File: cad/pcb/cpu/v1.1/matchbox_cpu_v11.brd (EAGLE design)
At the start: 40 x 32 mm, 61 parts, among them CN1 SM02B-SRSS-TB, P1 DF12-32-DP, P2 DF12-32-DP, Q1 FDN360P, Q2 FDN360P, U1 STM32F415R, U2 MCP1703, U3 MCP73831, U4 LTC2954-2, Y1 16MHz(9pF)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

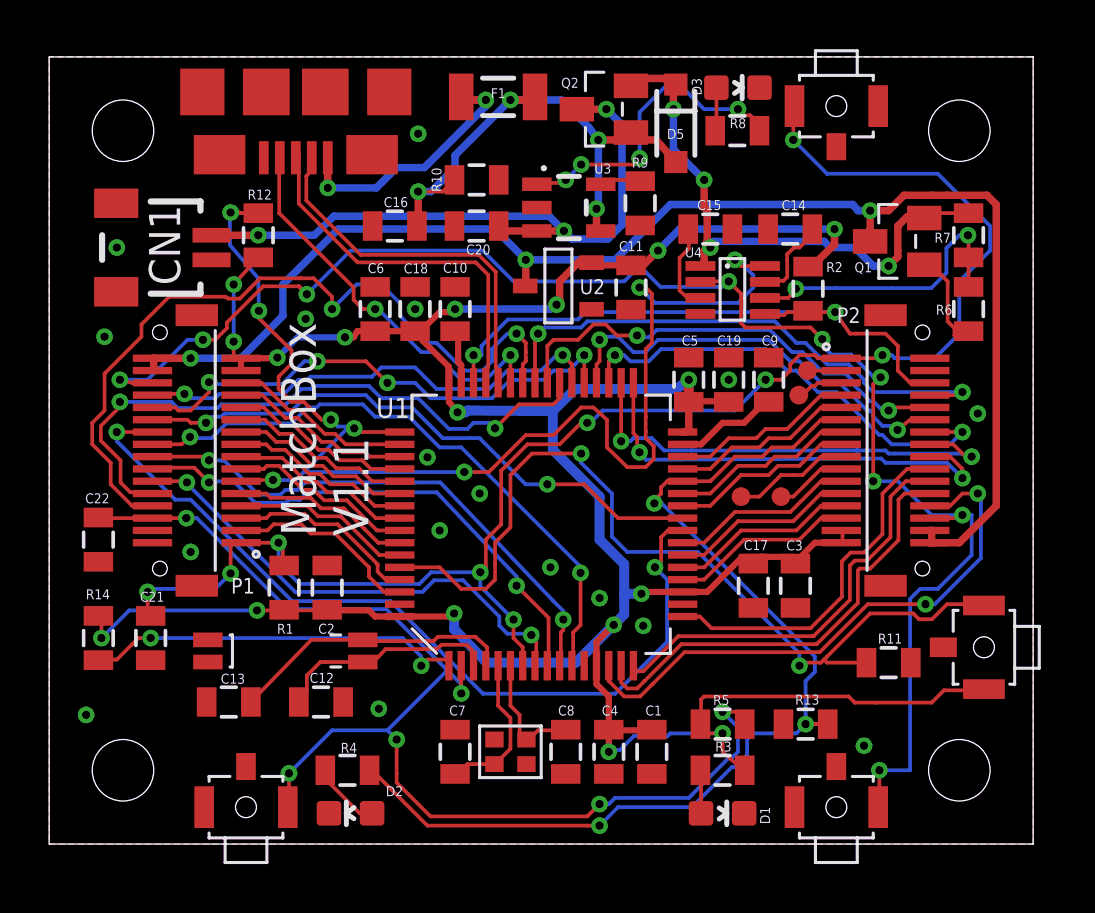
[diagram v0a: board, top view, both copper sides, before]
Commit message: Side button improvement
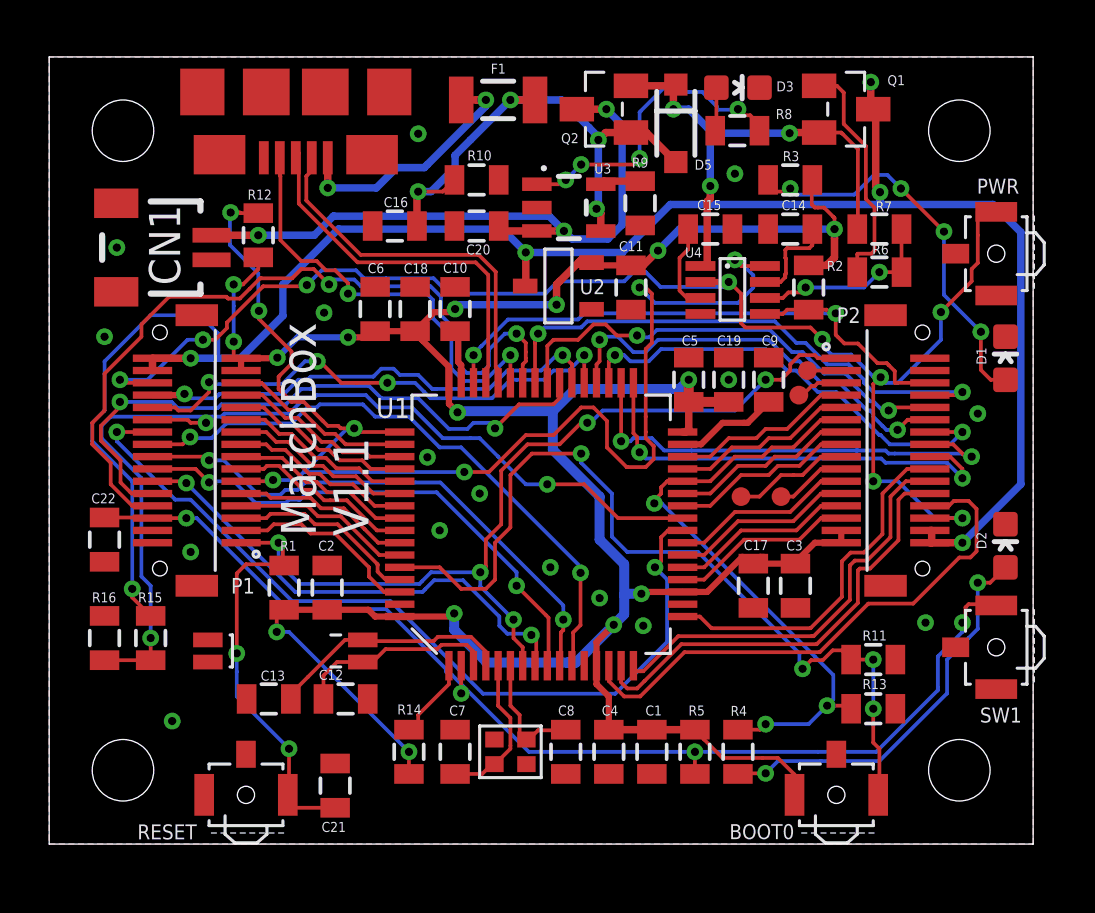
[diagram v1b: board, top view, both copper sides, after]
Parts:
- removed U$2, U$3, U$4, U$5: B3U-3100PM-B, sharp_display:B3U-3100PM-B
- added BOOT0, PWR, RESET, SW1: B3U-3100PM-B, sharp_display:B3U-3100PM-B
- added R15, R16: 10k, SparkFun-Passives:0805
- D2: value PB2 -> STAT
- moved D2 28.8 mm to (38.9, 12.1), turned to 0 degrees
- moved R3 24.2 mm to (30.1, 27.0)
- moved D1 21.8 mm to (38.9, 19.8), turned to 0 degrees
- moved R4 15.9 mm to (28.0, 3.75), turned to 90 degrees
- moved R14 13.4 mm to (14.6, 3.75), turned to 90 degrees
- moved C21 9.60 mm to (11.6, 2.38), turned to 90 degrees
- moved Q1 5.76 mm to (32.4, 29.9), turned to 270 degrees
- moved R6 3.92 mm to (33.8, 23.2), turned to 0 degrees
- moved R7 3.63 mm to (33.8, 25.0), turned to 0 degrees
- moved R13 2.82 mm to (33.5, 5.50), turned to 0 degrees
- moved C13 1.63 mm to (8.93, 5.90)
- moved R5 1.59 mm to (26.2, 3.75), turned to 90 degrees
- moved C12 1.01 mm to (12.1, 5.90)
- moved R11 0.64 mm to (33.5, 7.50)
- moved C22 0.25 mm to (2.25, 12.4)
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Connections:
- net BOOT0: now also BOOT0.1; no longer U$5.1
- net GND: now also BOOT0.GND, PWR.2, PWR.GND, R16.2, RESET.2, RESET.GND, SW1.2, SW1.GND; no longer U$2.2, U$2.GND, U$3.2, U$3.GND, U$4.2, U$4.GND, U$5.GND
- net PC13: now also SW1.1; no longer U$3.1
- net PC5: now also R15.2, R16.1
- net PWR_ON: now also PWR.1; no longer U$4.1
- net RESET#: now also RESET.1; no longer U$2.1
- net VCC: now also R15.1
- net VCC_3V3: now also BOOT0.2; no longer U$5.2
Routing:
- net VCC: track 58.9 -> 80.7 mm, vias 3 -> 6
- net PB2: track 44.1 -> 26.1 mm
- net PC5: track 24.1 -> 41.5 mm, vias 2 -> 3
- net RESET#: track 67.9 -> 51.7 mm, vias 9 -> 7
- net N$5: track 1.76 -> 16.5 mm, vias 0 -> 4
- net N$6: track 2.85 -> 16.3 mm, vias 0 -> 2
- net VCC_3V3: track 129.3 -> 116.2 mm, vias 17 -> 15
- net VCC_BKUP: track 15.8 -> 3.54 mm, vias 2 -> 0
- net PWR_ON: track 65.1 -> 59.0 mm
- net N$8: track 12.8 -> 8.04 mm
- net VCC_SEL: track 24.8 -> 20.3 mm, vias 4 -> 3
- net N$9: track 5.12 -> 9.54 mm
- net PC13: track 50.6 -> 46.7 mm, vias 6 -> 4
- net BOOT0: track 37.7 -> 35.4 mm, vias 2 -> 4
- net PA10: track 16.4 -> 18.2 mm
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
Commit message: Change capacitance values. Final build?
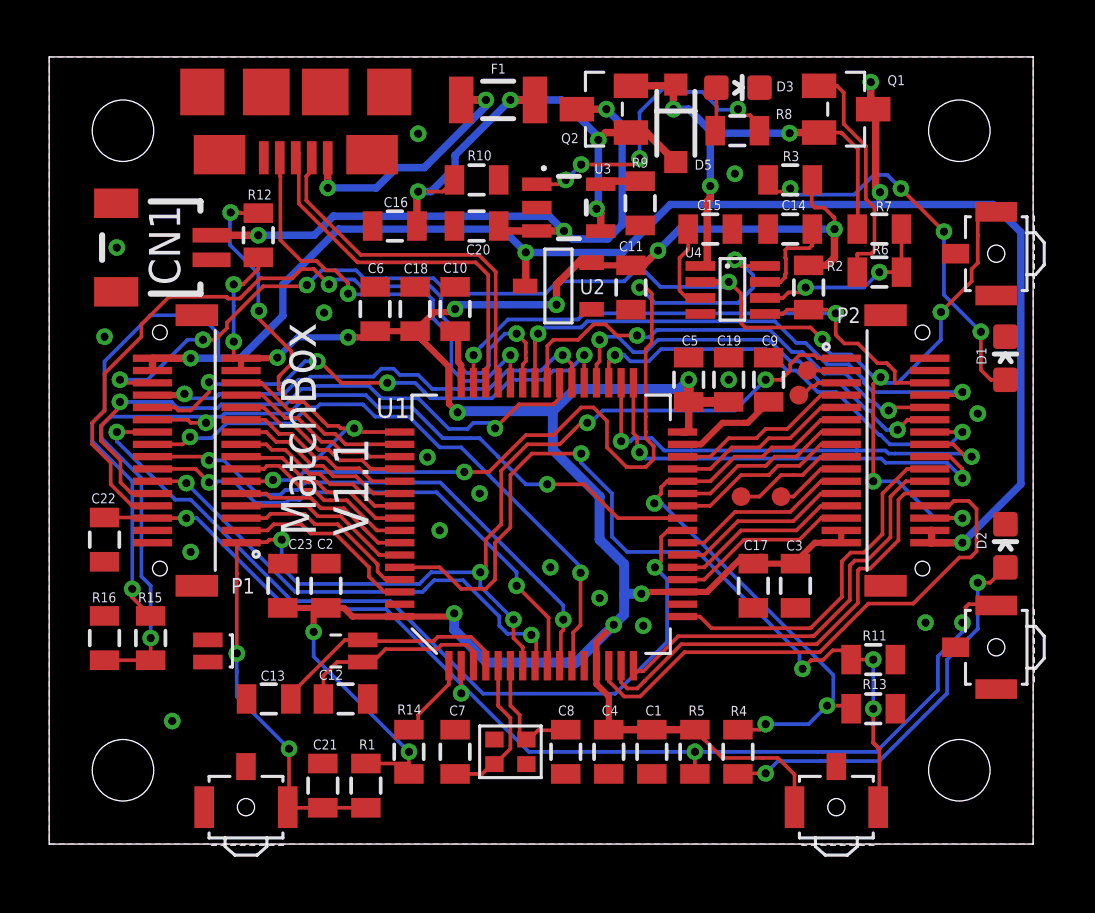
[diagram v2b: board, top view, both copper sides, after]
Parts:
- added C23: 1uF, SparkFun-Capacitors:0805
- C2: value 1uF -> 0.1uF
- moved R1 8.71 mm to (12.9, 2.38), turned to 90 degrees
- moved BOOT0 0.50 mm to (32.0, 1.50)
- moved C21 0.50 mm to (11.1, 2.38)
- moved RESET 0.50 mm to (8.00, 1.50)
- moved C2 0.09 mm to (11.2, 10.5)
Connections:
- net GND: now also C23.2
- net VCC_3V3: now also C23.1
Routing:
- net VCC_3V3: track 116.2 -> 118.4 mm
- net BOOT0: track 35.4 -> 36.2 mm
